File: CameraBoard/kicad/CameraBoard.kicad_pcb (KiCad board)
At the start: 2 copper layers, 101.6 x 76.2 mm, 56 parts, among them Q1 SUD08P06-155L, Q2 SUD08P06-155L, Q3 SUD08P06-155L, U1 LM2678SD-12/NOPB, U1 MP2659GQ-0000-Z

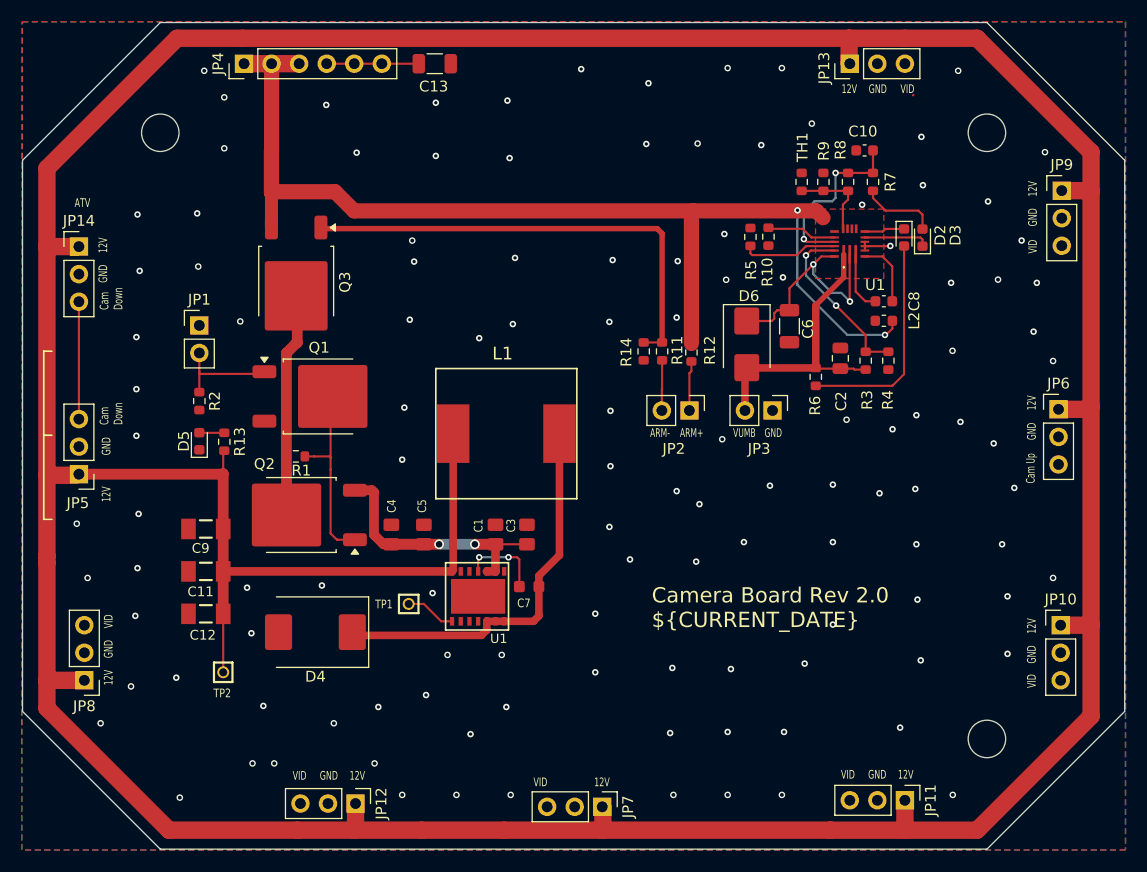
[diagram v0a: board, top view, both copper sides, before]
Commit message: Small updates to PCB
-Made text the same size
-Changed U1 symbol
-Added zones
-Moved connectors to more convenient location
-Moved leds together
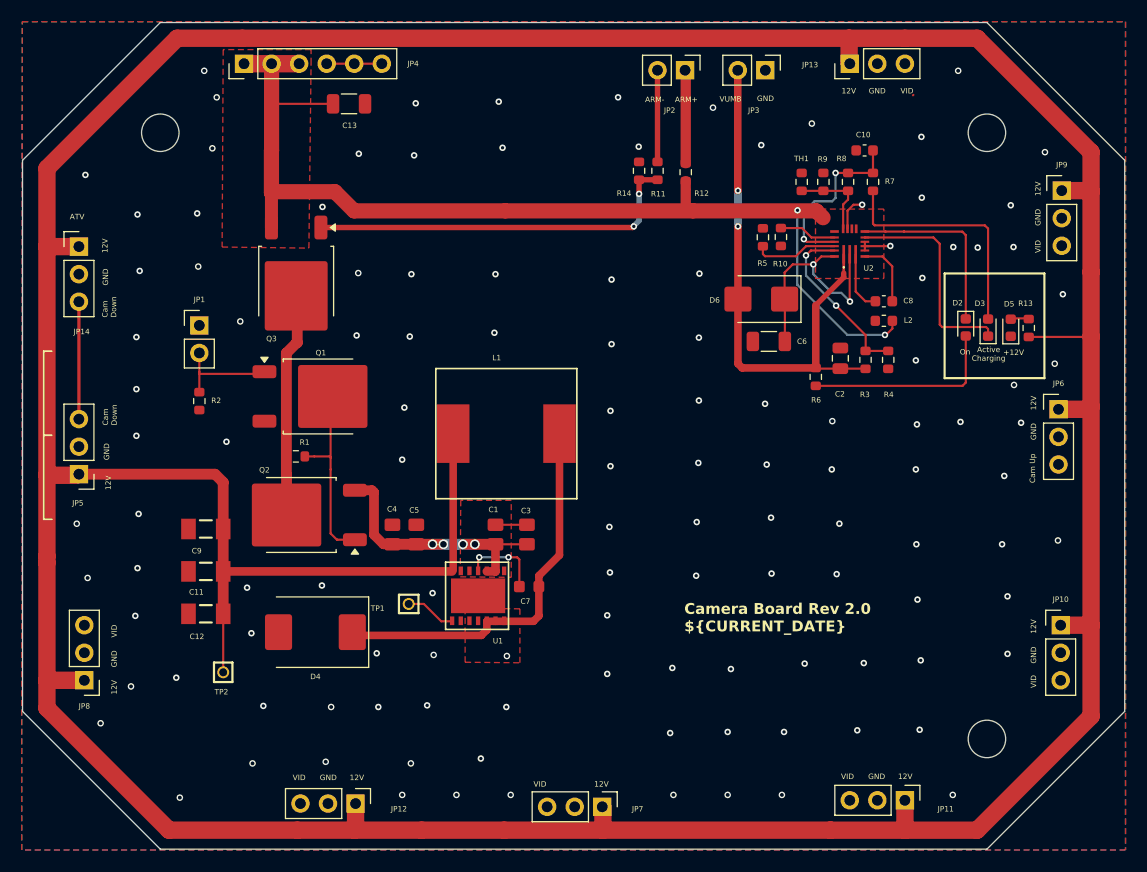
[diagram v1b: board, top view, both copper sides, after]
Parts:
- U1: value LM2678SD-12/NOPB -> ~
- moved D5 75.5 mm to (188.8, 95.0)
- moved R13 74.9 mm to (190.5, 95.1)
- moved JP3 31.4 mm to (166.2, 71.3)
- moved JP2 31.4 mm to (158.8, 71.3)
- moved R14 16.6 mm to (154.5, 80.6), turned to 90 degrees
- moved R11 16.6 mm to (156.2, 80.6), turned to -90 degrees
- moved R12 16.6 mm to (158.8, 80.7), turned to -90 degrees
- moved D3 10.3 mm to (186.7, 95.0)
- moved D2 10.1 mm to (184.7, 95.0)
- moved C13 8.72 mm to (127.8, 74.4)
- moved D6 4.38 mm to (165.8, 92.4), turned to 180 degrees
- moved C6 2.36 mm to (166.5, 96.3), turned to 0 degrees
- moved R10 1.15 mm to (167.6, 86.7)
- moved R5 1.15 mm to (165.9, 86.7)
- moved C5 0.70 mm to (134.0, 114.1)
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- renumbered U1 to U2
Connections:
- C13 pad 1: Net-(JP4-Pin_4) -> /BATT+
- JP4 pad 4: Net-(JP4-Pin_4) -> GND
- JP4 pad 5: Net-(JP4-Pin_4) -> GND
- JP4 pad 6: Net-(JP4-Pin_4) -> GND
- JP6 pad 3: /CAM_UP -> unconnected-(JP6-Pin_3-Pad3)
- U1 pad 1: (no net) -> unconnected-(U1-NC-Pad1)
- U1 pad 10: (no net) -> unconnected-(U1-NC-Pad10)
- U1 pad 11: (no net) -> unconnected-(U1-NC-Pad11)
- U1 pad 5: (no net) -> unconnected-(U1-NC-Pad5)
- U1 pad 6: (no net) -> unconnected-(U1-NC-Pad6)
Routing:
- net /VUMB: track 26.2 -> 50.2 mm, vias 0 -> 2
- net Net-(D3-A): track 7.19 -> 22.2 mm
- net Net-(D3-K): track 6.00 -> 19.9 mm
- net Net-(D2-K): track 3.71 -> 17.2 mm
- net GND: track 3.21 -> 14.4 mm
- net Net-(JP4-Pin_4): track 8.48 -> 0.00 mm
- net Net-(Q3-G): track 43.4 -> 35.1 mm, vias 0 -> 2
- net /ARM-OUT: track 4.60 -> 8.60 mm
- net /ARM-IN: track 4.64 -> 8.59 mm
- net +12V: track 407.8 -> 411.7 mm
- net /BATT+: track 102.7 -> 98.9 mm
- net Net-(D2-A): track 20.4 -> 18.2 mm
- net Net-(Q2-S): track 23.9 -> 25.7 mm, vias 2 -> 4
- net Net-(U2-ISET): track 6.42 -> 5.30 mm
- net Net-(U2-ILIM): track 8.85 -> 7.79 mm
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- added copper zone on F.Cu, net /SOUT
- added copper zone on F.Cu, net VBATT
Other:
- board text added: "+12V"
- board text added: "Active Charging"
- board text added: "On"

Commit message: Small Updates to PCB
-Fixed zone issue
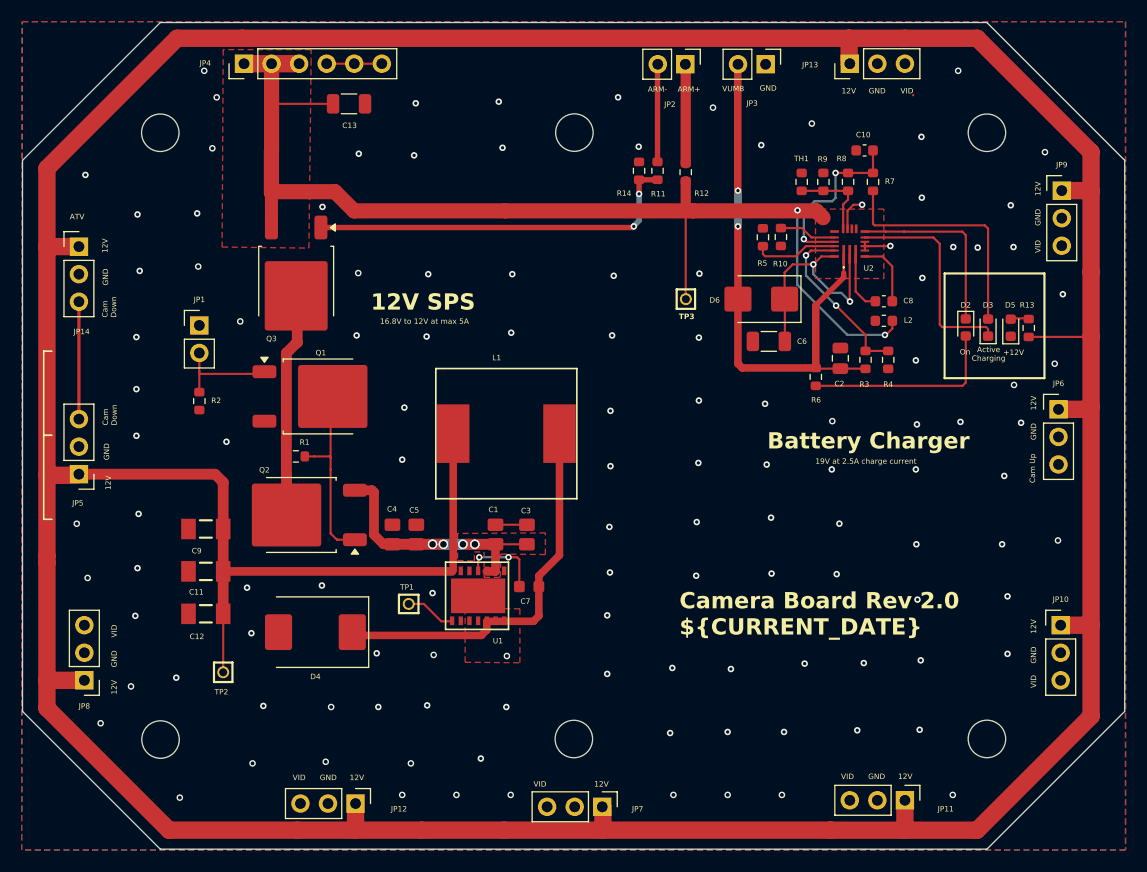
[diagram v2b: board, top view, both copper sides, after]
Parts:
- added TP3: Test-Point, CameraBoard:2MM-TEST-POINT, F.Cu at (158.8, 92.4)
- moved JP2 0.55 mm to (158.8, 70.8)
- moved JP3 0.55 mm to (166.2, 70.8)
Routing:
- net /BATT+: track 98.9 -> 107.1 mm
- net /ARM-IN: track 8.59 -> 9.75 mm
- net +12V: track 411.7 -> 411.0 mm
- net /VUMB: track 50.2 -> 50.7 mm
- net /ARM-OUT: track 8.60 -> 9.15 mm
- added copper zone on F.Cu, net Net-(Q2-S)
- removed copper zone on F.Cu, net VBATT
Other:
- outline, holes or cut-outs redrawn
- board text added: "12V SPS"
- board text added: "16.8V to 12V at max 5A"
- board text added: "19V at 2.5A charge current"
- board text added: "Battery Charger"

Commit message: Updates to BOM and Footprints
-Inductor and thermistor had wrong footprints
-Had to change layout and reroute traces for footprints
-Filled out BOM from schematic
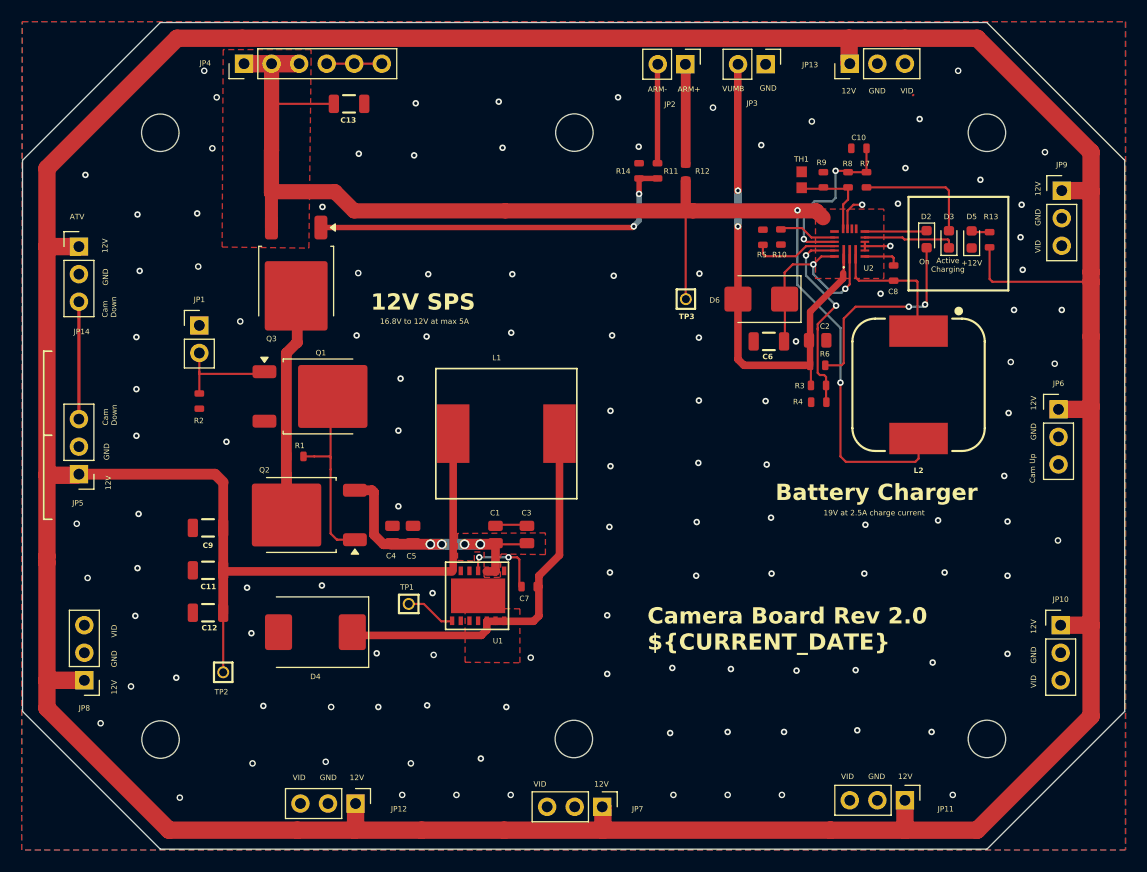
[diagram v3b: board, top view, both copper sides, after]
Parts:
- C1, C3, C4, C5: footprint CameraBoard:.0805-B-NOSILK -> oresat-passives:0805-C-NOSILK
- C10, C8: footprint Capacitor_SMD:C_0603_1608Metric -> oresat-passives:0603-C-NOSILK
- C11, C12, C9: footprint CameraBoard:1206-A -> oresat-passives:1206-C
- C13, C6: footprint Capacitor_SMD:C_1206_3216Metric -> oresat-passives:1206-C
- C2: footprint Capacitor_SMD:C_0805_2012Metric -> oresat-passives:0805-C-NOSILK
- C7: footprint CameraBoard:.0603-A-NOSILK -> oresat-passives:0603-C-NOSILK
- L2: footprint Inductor_SMD:L_0603_1608Metric -> oresat-misc:WE-PD_1260
- R1, R10, R11, R12, R13, R14, R2, R3, R4, R5, R6, R7, R8, R9: footprint Resistor_SMD:R_0603_1608Metric -> oresat-passives:0603-C-NOSILK
- TH1: footprint Resistor_SMD:R_0603_1608Metric -> oresat-misc:THRMC1608X95N
- moved D2 8.90 mm to (181.0, 86.9)
- moved D3 8.90 mm to (183.1, 86.9)
- moved R13 8.90 mm to (186.8, 86.9)
- moved D5 8.90 mm to (185.2, 86.9)
- moved R4 7.49 mm to (171.1, 101.9), turned to 0 degrees
- moved L2 6.71 mm to (180.3, 100.3), turned to 180 degrees
- moved R3 4.93 mm to (171.1, 100.4), turned to 180 degrees
- moved C8 2.75 mm to (178.0, 90.0), turned to -90 degrees
- moved C2 2.67 mm to (171.0, 96.2), turned to 0 degrees
- moved R6 1.08 mm to (171.0, 98.5), turned to 0 degrees
- moved R7 0.63 mm to (175.5, 81.4)
- moved C10 0.56 mm to (174.8, 78.5)
- moved C5 0.30 mm to (133.7, 114.1)
- moved C9 0.22 mm to (114.8, 113.5)
- moved C11 0.22 mm to (114.8, 117.4)
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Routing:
- net /BATT+: track 107.1 -> 122.3 mm
- net Net-(D2-K): track 17.2 -> 5.73 mm
- net Net-(D3-K): track 19.9 -> 8.83 mm
- net Net-(D3-A): track 22.2 -> 11.7 mm
- net Net-(U2-SW): track 5.63 -> 12.6 mm
- net +12V: track 411.0 -> 417.6 mm
- net /VUMB: track 50.7 -> 47.1 mm
- net Net-(U2-VDPM): track 16.1 -> 18.9 mm
- net Net-(U2-BST): track 6.13 -> 3.40 mm
- net Net-(D6-K): track 21.4 -> 19.6 mm
- net Net-(D2-A): track 18.2 -> 19.2 mm, vias 0 -> 2
- net Net-(Q2-S): track 25.6 -> 26.3 mm
- net GND: vias 122 -> 120

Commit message: Small Updates to PCB
- Increased battery trace width
- Created zone for 12V supply
- Moved led resistor outside box
- Rearranged mosfets and capacitors to look nicer
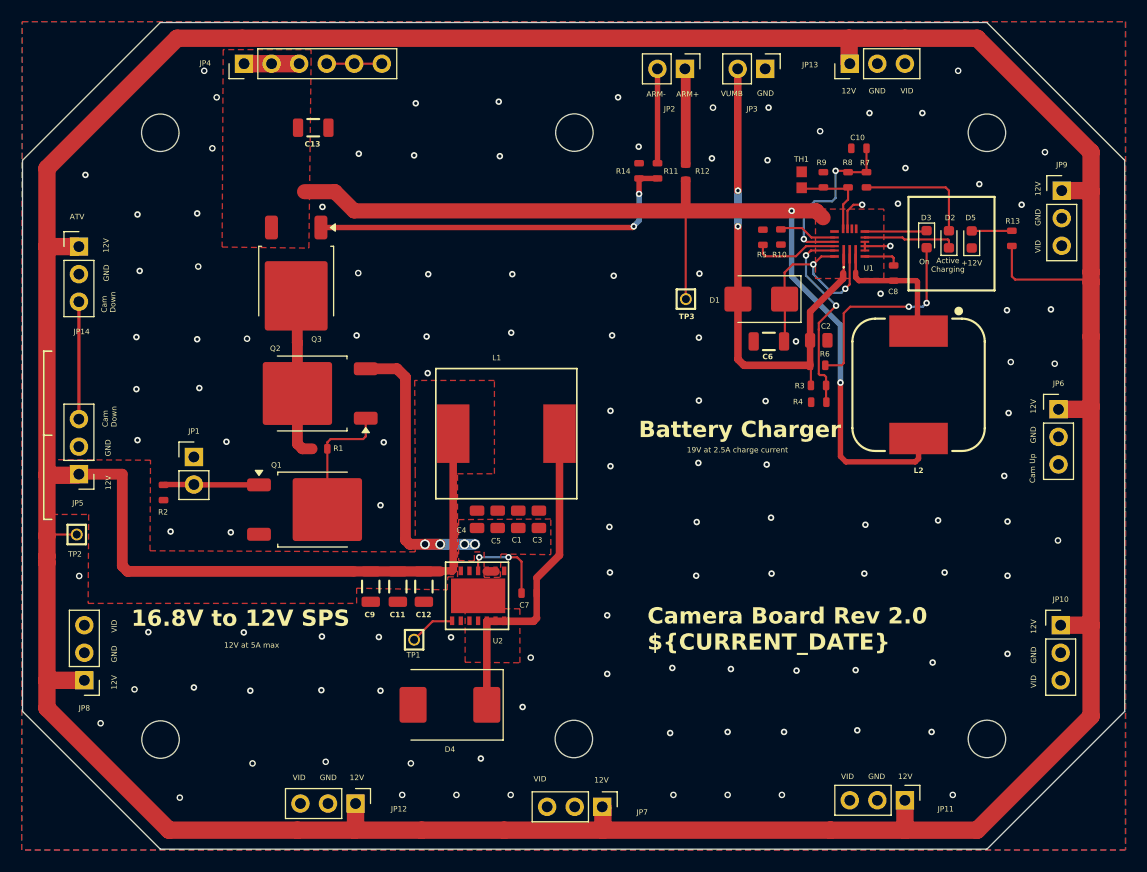
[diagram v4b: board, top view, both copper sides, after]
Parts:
- moved C12 20.0 mm to (134.7, 118.9), turned to -90 degrees
- moved TP2 18.5 mm to (102.7, 114.1)
- moved C11 17.6 mm to (132.3, 118.9), turned to -90 degrees
- moved C9 15.9 mm to (129.8, 118.9), turned to -90 degrees
- moved D4 14.1 mm to (137.1, 129.8)
- moved JP1 12.1 mm to (113.5, 107.0)
- moved Q2 11.2 mm to (124.3, 101.1)
- moved Q1 10.4 mm to (124.5, 111.8)
- moved R2 9.05 mm to (110.7, 110.2)
- moved C5 7.92 mm to (141.5, 112.7)
- moved C4 7.92 mm to (139.6, 112.7)
- moved C13 3.97 mm to (124.5, 76.6)
- moved TP1 3.34 mm to (133.8, 123.8), turned to 180 degrees
- moved C1 2.52 mm to (143.4, 112.7)
- moved R1 2.31 mm to (125.1, 106.2)
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- renumbered D6 to D1, U2 to U1, U1 to U2
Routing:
- net /BATT+: track 122.3 -> 98.8 mm
- net +12V: track 417.6 -> 408.9 mm
- net /SOUT: track 36.1 -> 30.3 mm
- net Net-(Q1-D): track 17.3 -> 11.6 mm
- net VBATT: track 20.7 -> 15.2 mm
- net GND: track 14.4 -> 11.5 mm, vias 120 -> 119
- net Net-(D5-A): track 1.70 -> 3.71 mm
- net Net-(Q2-S): track 26.3 -> 27.7 mm
- net /ARM-IN: track 9.75 -> 8.99 mm
- net Net-(U2-CB): track 7.62 -> 8.31 mm
- net Net-(JP1-Pin_2): track 9.41 -> 8.83 mm
- added copper zone on F.Cu, net +12V
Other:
- board text added: "12V at 5A max"
- board text added: "16.8V to 12V SPS"
- board text removed: "12V SPS"
- board text removed: "16.8V to 12V at max 5A"
